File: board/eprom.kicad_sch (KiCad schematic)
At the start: 15 parts, among them J201 Conn_02x21_Counter_Clockwise, U201 MCP23008-E/SS, U202 MCP23008-E/SS, U203 MCP23008-E/SS, U204 MCP23008-E/SS, U205 MCP23008-E/SS, U251 PCA9306DCTR

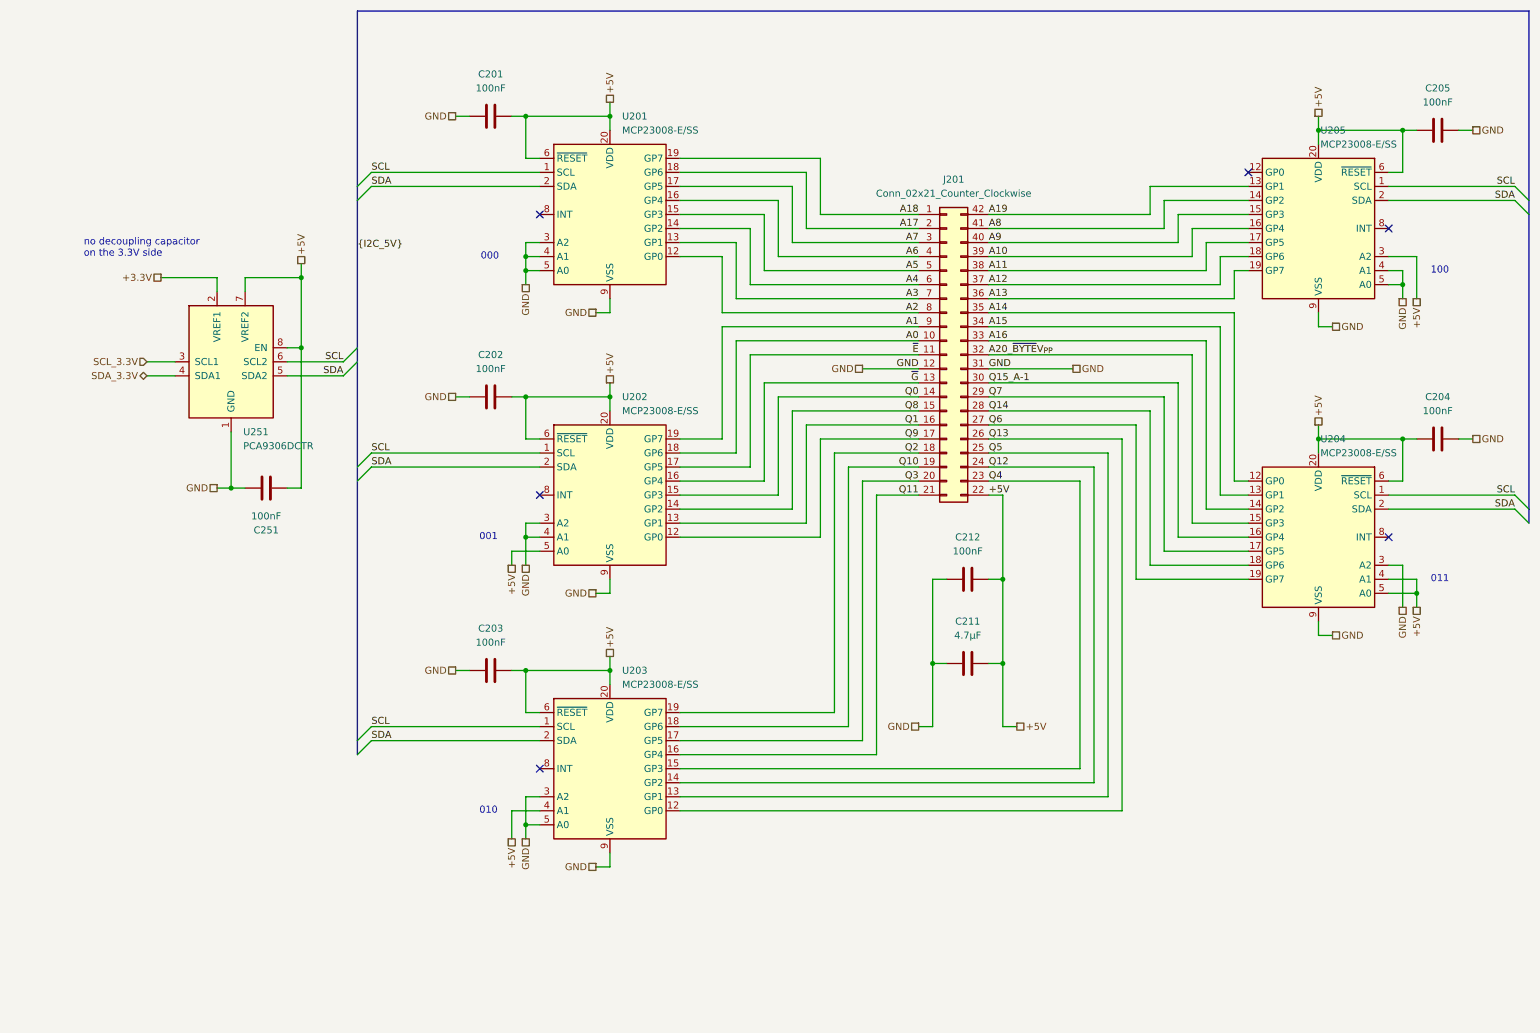
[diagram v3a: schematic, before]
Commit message: allow driving ~RESET pins of I2C I/O expanders, add missing resistors
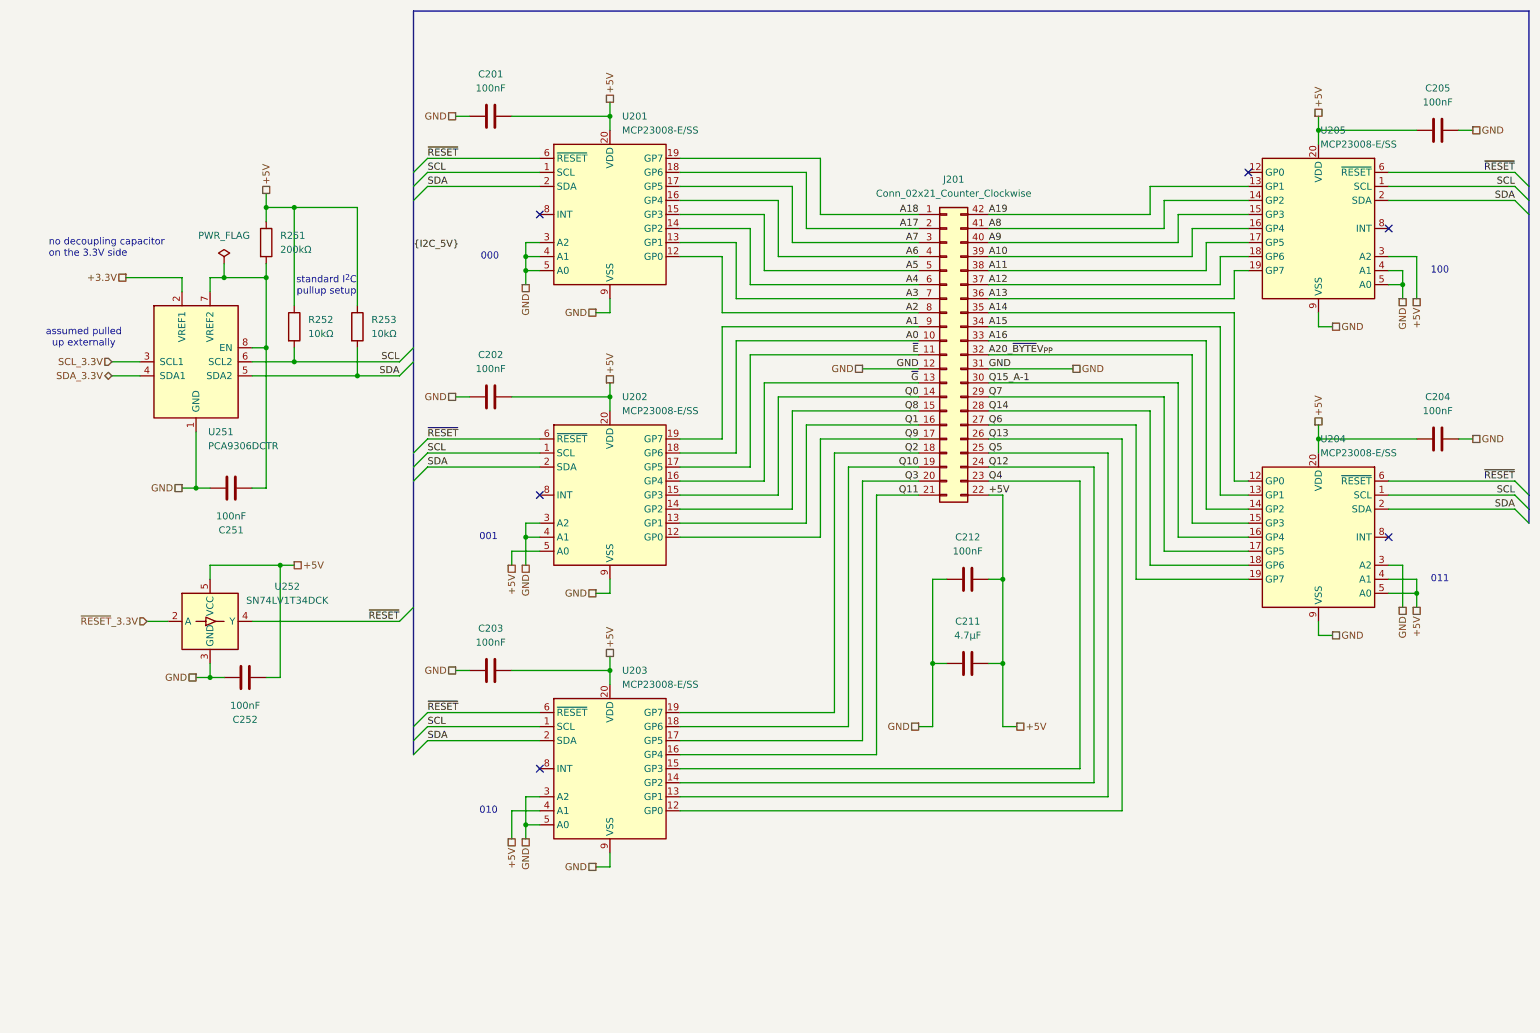
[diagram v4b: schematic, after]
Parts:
- added C252: 100nF, Capacitor_SMD:C_0402_1005Metric, symbol Device:C
- added R251: 200kΩ, Resistor_SMD:R_0402_1005Metric, symbol Device:R
- added R252, R253: 10kΩ, Resistor_SMD:R_0402_1005Metric, symbol Device:R
- added U252: SN74LV1T34DCK, Package_TO_SOT_SMD:SOT-353_SC-70-5, symbol Logic_LevelTranslator:SN74LV1T34DCK
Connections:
- net +5V: now also C252.2, R251.1, R252.1, R253.1, U252.5 (VCC); no longer C251.2, U201.6 (~{RESET}), U202.6 (~{RESET}), U203.6 (~{RESET}), U204.6 (~{RESET}), U205.6 (~{RESET}), U251.7 (VREF2), U251.8 (EN)
- net GND: now also C252.1, U252.3 (GND)
- net SCL: now also R252.2
- net SDA: now also R253.2
- new net: C251.2, R251.2, U251.7 (VREF2), U251.8 (EN)
- new net ~{RESET}: U201.6 (~{RESET}), U202.6 (~{RESET}), U203.6 (~{RESET}), U204.6 (~{RESET}), U205.6 (~{RESET}), U252.4 (Y)
- new net ~{RESET}_3.3V: U252.2 (A)
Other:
- note added: "assumed pulled up externally"
- note added: "standard I^{2}C pullup setup"
- moved on the sheet: C251, U251
